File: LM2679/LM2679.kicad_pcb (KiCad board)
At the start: 2 copper layers, 61.2 x 36.8 mm, 15 parts, among them J1 - INPUT +, J2 + OUTPUT -, U1 LM2679SX-5.0/NOPB

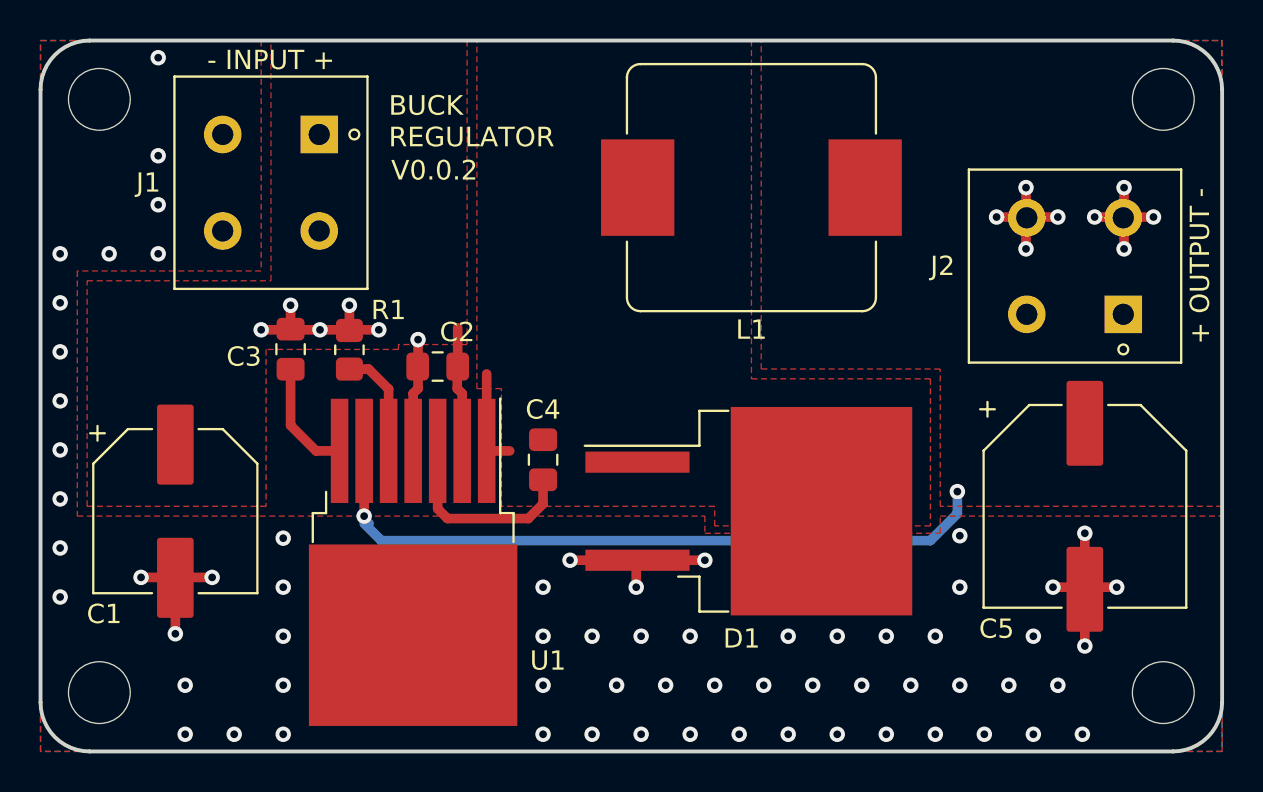
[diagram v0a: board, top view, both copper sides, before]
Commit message: Inductor changed
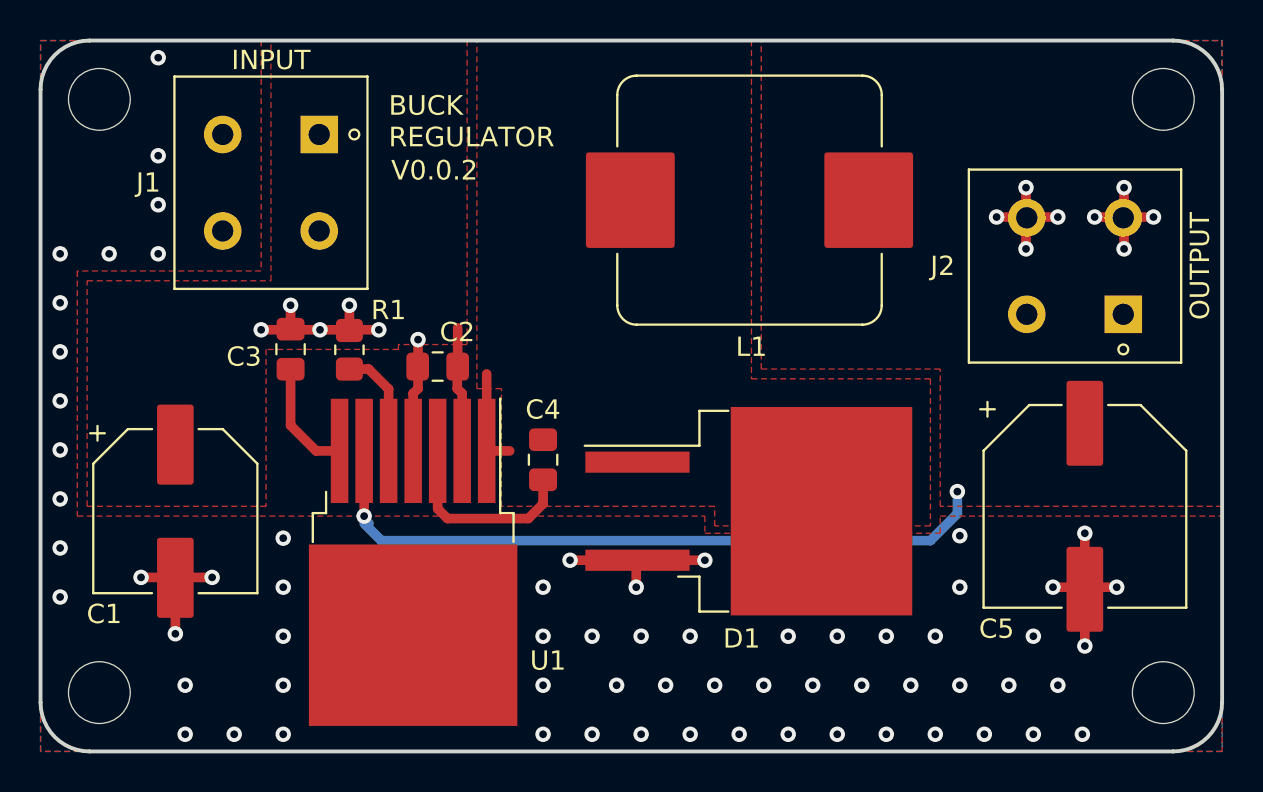
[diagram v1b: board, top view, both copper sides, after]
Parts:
- J1: value - INPUT + -> INPUT
- J2: value + OUTPUT - -> OUTPUT
- L1: footprint Inductor_SMD:L_Bourns_SRP1245A -> Inductor_SMD:L_Vishay_IHLP-5050_HandSolder
- moved L1 0.63 mm to (154.7, 83.7)

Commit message: Changes to silkscreen
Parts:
- J1: value INPUT -> - INPUT +
- J2: value OUTPUT -> + OUTPUT -
